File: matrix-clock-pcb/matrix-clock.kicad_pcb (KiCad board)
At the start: 2 copper layers, 40 x 65 mm, 45 parts, among them J1 download, J2 Conn_02x08_Counter_Clockwise, J3 Conn_01x02, J4 USB_C_Receptacle_USB2.0, J5 Speaker, Q1 MMBT5551L, Q2 MMBT5551L, U1 ESP32-WROOM-32D, U2 SHTC3, U3 TXB0108PWR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

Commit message: pcb: update pcb to v1.1
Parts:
- R12: value 20k -> 10k
- U3, U4: value TXB0108PWR -> 74HC245
- moved C6 7.97 mm to (161.5, 96.3)
- moved C5 6.10 mm to (159.3, 104.0)
- moved U3 0.10 mm to (156.4, 99.2)
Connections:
- C5 pad 2: +3V3 -> +5V
- U3 pad 1: /LED_SCK -> +5V
- U3 pad 10: +3V3 -> GND
- U3 pad 11: GND -> /_LED_A
- U3 pad 12: /_LED_A -> /_LED_B
- U3 pad 13: /_LED_B -> /_LED_C
- U3 pad 14: /_LED_C -> /_LED_D
- U3 pad 15: /_LED_D -> /_LED_G1
- U3 pad 16: /_LED_G1 -> /_LED_G2
- U3 pad 17: /_LED_G2 -> /_LED_STCP
- U3 pad 18: /_LED_STCP -> /_LED_SCK
- U3 pad 19: +5V -> GND
- U3 pad 2: +3V3 -> /LED_SCK
- U3 pad 20: /_LED_SCK -> +5V
- U4 pad 1: /LED_R2 -> +5V
- U4 pad 10: +3V3 -> GND
- U4 pad 11: GND -> Net-(U4-Pad11)
- U4 pad 16: Net-(U4-Pad16) -> /_LED_OE
- U4 pad 17: /_LED_OE -> /_LED_R1
- U4 pad 18: /_LED_R1 -> /_LED_R2
- U4 pad 19: +5V -> GND
- U4 pad 2: +3V3 -> /LED_R2
- U4 pad 20: /_LED_R2 -> +5V
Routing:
- net GND: track 44.6 -> 65.9 mm, vias 69 -> 60
- net +3V3: track 134.5 -> 121.5 mm, vias 9 -> 7
- net +5V: track 82.8 -> 79.8 mm, vias 2 -> 7
- net /LED_SCK: track 7.42 -> 9.91 mm
- net /_LED_R2: track 10.7 -> 11.2 mm
- net /LED_R2: track 18.1 -> 18.6 mm
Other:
- outline, holes or cut-outs redrawn

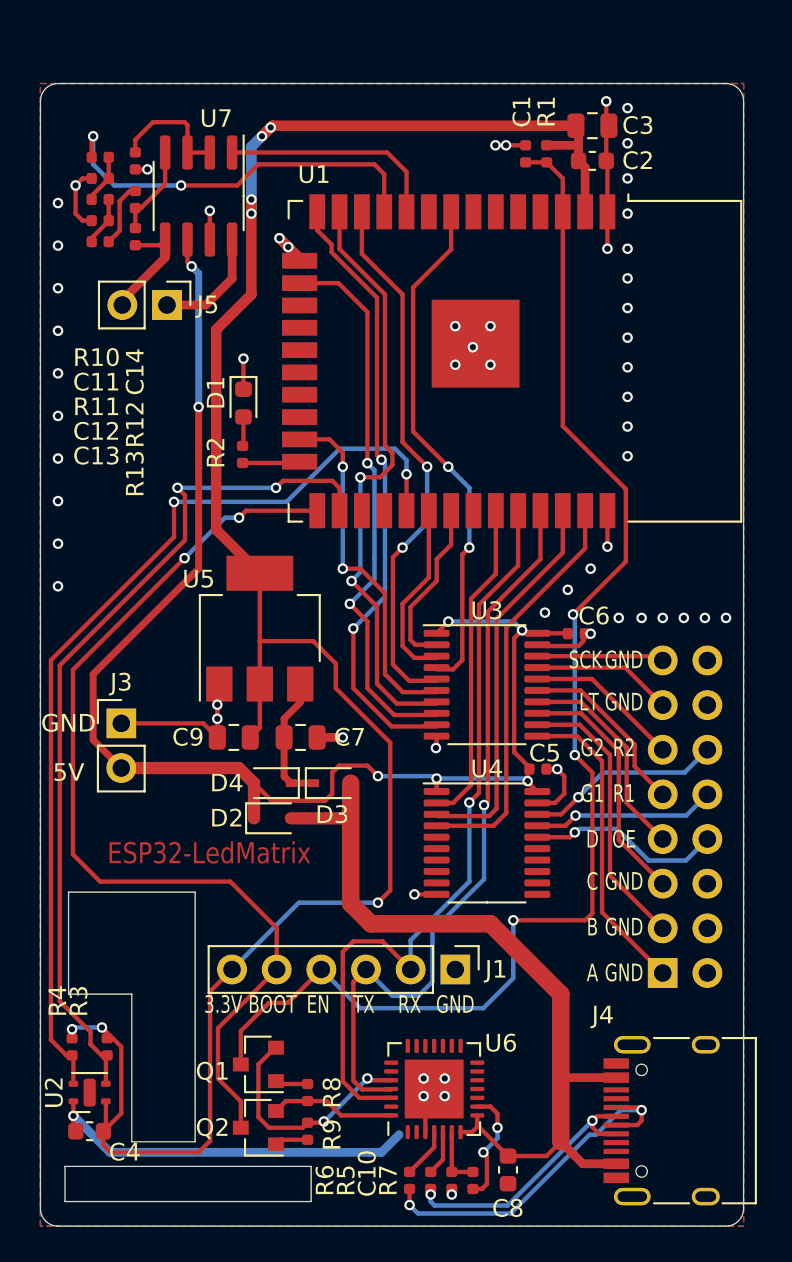
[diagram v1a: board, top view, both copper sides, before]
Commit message: fix(pcb): update pcb layout
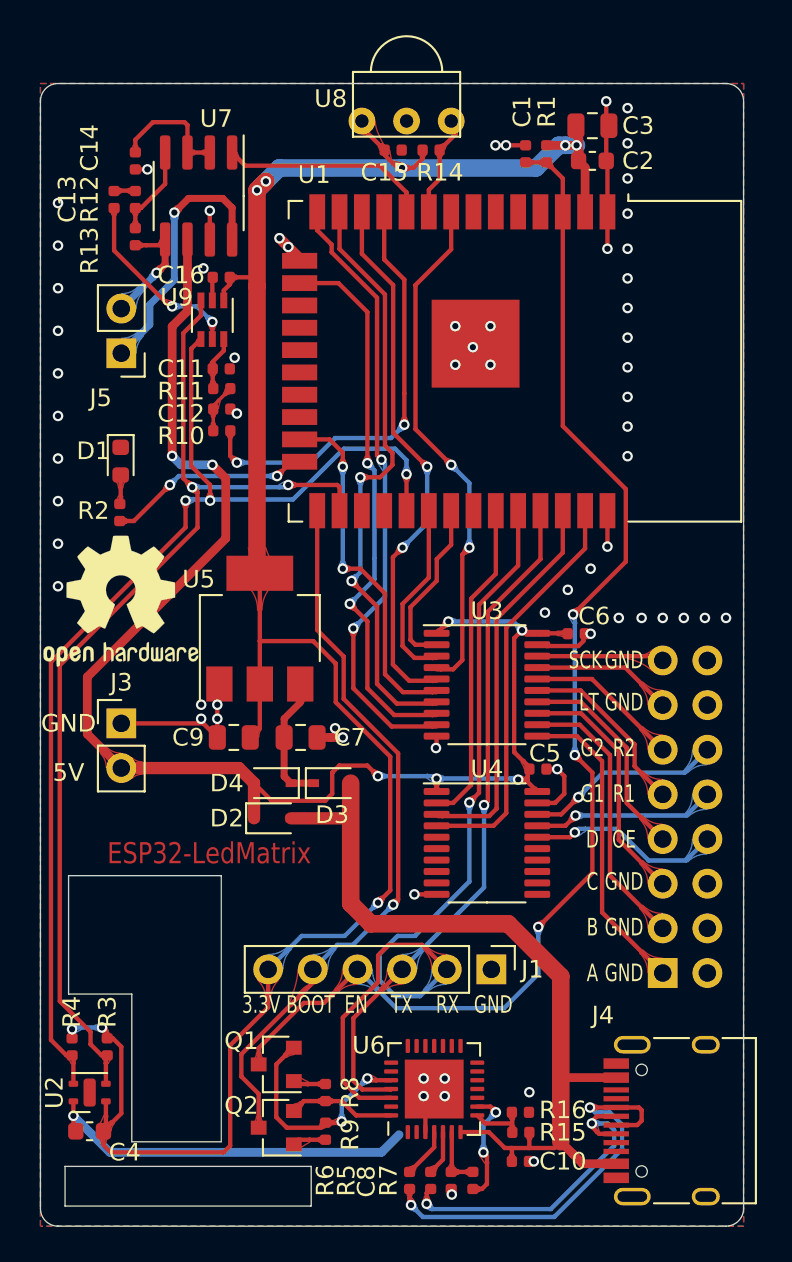
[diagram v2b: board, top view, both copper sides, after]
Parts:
- added C15: 0.1uf, Capacitor_SMD:C_0402_1005Metric, F.Cu at (151.1, 68.8)
- added C16: 0.1uf, Capacitor_SMD:C_0402_1005Metric, F.Cu at (141.3, 76.0)
- added R14: 10K, Resistor_SMD:R_0402_1005Metric, F.Cu at (153.2, 68.8)
- added R15: 24k, Resistor_SMD:R_0402_1005Metric, F.Cu at (158.3, 124.7)
- added R16: 47k, Resistor_SMD:R_0402_1005Metric, F.Cu at (158.3, 123.5)
- added REF**: OSHW-Logo2_9.8x8mm_SilkScreen, Symbol:OSHW-Logo2_9.8x8mm_SilkScreen, F.Cu at (135.6, 94.4)
- added U8: VS1838, esp32:Infrared_Receiver_module, F.Cu at (151.8, 66.5)
- added U9: TPL0401A-10-Q1, Package_TO_SOT_SMD:Texas_R-PDSO-G6, F.Cu at (140.8, 78.4)
- C10: value 0.1uf -> 1uf
- C11: value 0.39uf -> 0.39uf(NC)
- C8: footprint Capacitor_SMD:C_0603_1608Metric -> Capacitor_SMD:C_0402_1005Metric
- moved R10 17.0 mm to (141.3, 84.8), turned to 0 degrees
- moved C11 12.8 mm to (141.3, 81.2), turned to 180 degrees
- moved R11 12.8 mm to (141.3, 82.4), turned to 0 degrees
- moved C12 12.8 mm to (141.3, 83.5), turned to 180 degrees
- moved R2 7.73 mm to (135.5, 89.4)
- moved D1 7.73 mm to (135.6, 86.5)
- moved C10 4.05 mm to (158.3, 126.3), turned to 0 degrees
- moved J5 3.78 mm to (135.6, 80.3), turned to 180 degrees
- moved C8 3.29 mm to (154.4, 127.4), turned to 90 degrees
- moved C13 2.53 mm to (135.2, 71.6), turned to 270 degrees
- moved J1 2.05 mm to (156.7, 115.4)
- moved R8 1.02 mm to (147.2, 122.4)
- moved R9 1.02 mm to (147.2, 124.6)
- moved Q1 1.02 mm to (144.4, 120.8)
- moved Q2 1.02 mm to (144.4, 124.4)
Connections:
- net Net-(R3-Pad2) renamed /SCL
- net Net-(R4-Pad2) renamed /SDA
- C10 pad 1: GND -> VBUS
- C10 pad 2: Net-(C10-Pad2) -> GND
- C13 pad 2: Net-(C12-Pad2) -> Net-(C13-Pad2)
- C8 pad 1: VBUS -> GND
- C8 pad 2: GND -> Net-(C8-Pad2)
- R10 pad 1: Net-(C11-Pad2) -> Net-(C12-Pad2)
- R11 pad 1: Net-(C12-Pad2) -> Net-(C11-Pad2)
- R11 pad 2: Net-(C11-Pad2) -> Net-(C12-Pad2)
- R7 pad 2: Net-(C10-Pad2) -> Net-(C8-Pad2)
- U1 pad 9: Net-(U1-Pad9) -> /IR_SIGNAL
- U6 pad 6: Net-(C10-Pad2) -> Net-(C8-Pad2)
- U6 pad 8: VBUS -> Net-(R15-Pad2)
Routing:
- net /BOOT: track 54.9 -> 41.6 mm, vias 2 -> 1
- net Net-(C13-Pad2): track 0.00 -> 10.7 mm, vias 0 -> 2
- net /SCL: track 49.2 -> 59.7 mm
- net /SDA: track 54.3 -> 63.9 mm, vias 2 -> 3
- net Net-(R2-Pad2): track 3.27 -> 11.6 mm, vias 0 -> 2
- net Net-(J5-Pad1): track 6.55 -> 14.9 mm, vias 0 -> 1
- net /RXD0: track 43.9 -> 51.2 mm
- net /IR_SIGNAL: track 0.00 -> 5.80 mm
- net GND: track 65.9 -> 61.8 mm, vias 60 -> 66
- net /TXD0: track 43.1 -> 39.2 mm
- net Net-(J4-PadA7): track 15.3 -> 18.9 mm
- net +3V3: track 121.5 -> 125.1 mm, vias 7 -> 8
- net Net-(C8-Pad2): track 0.00 -> 3.46 mm
- net Net-(C10-Pad2): track 3.46 -> 0.00 mm
- net Net-(R15-Pad2): track 0.00 -> 3.32 mm
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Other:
- outline, holes or cut-outs redrawn
